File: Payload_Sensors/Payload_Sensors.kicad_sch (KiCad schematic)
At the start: 54 parts, among them J1 Conn_01x06_Pin, U1 MCP9601-E/MX, U2 MCP9601-E/MX, U3 MCP9601-E/MX, U4 MCP9601-E/MX, U5 MCP9601-E/MX

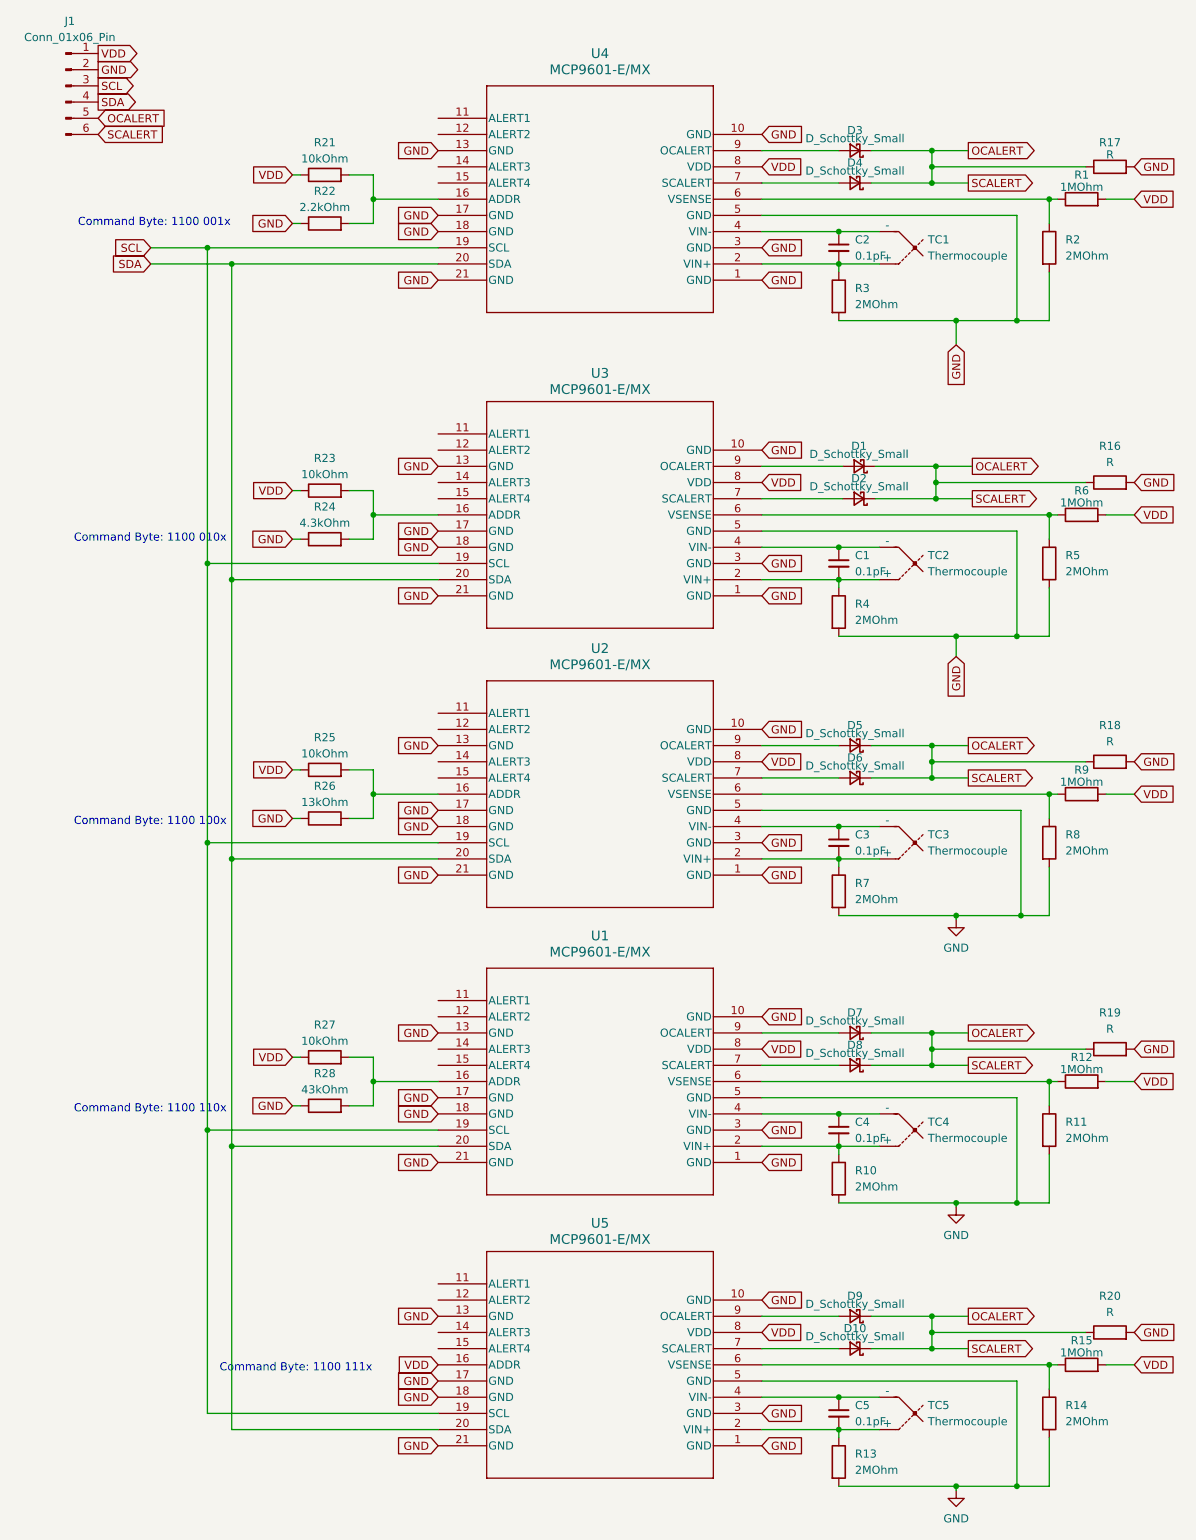
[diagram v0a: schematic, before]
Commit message: using hierarchical sheet
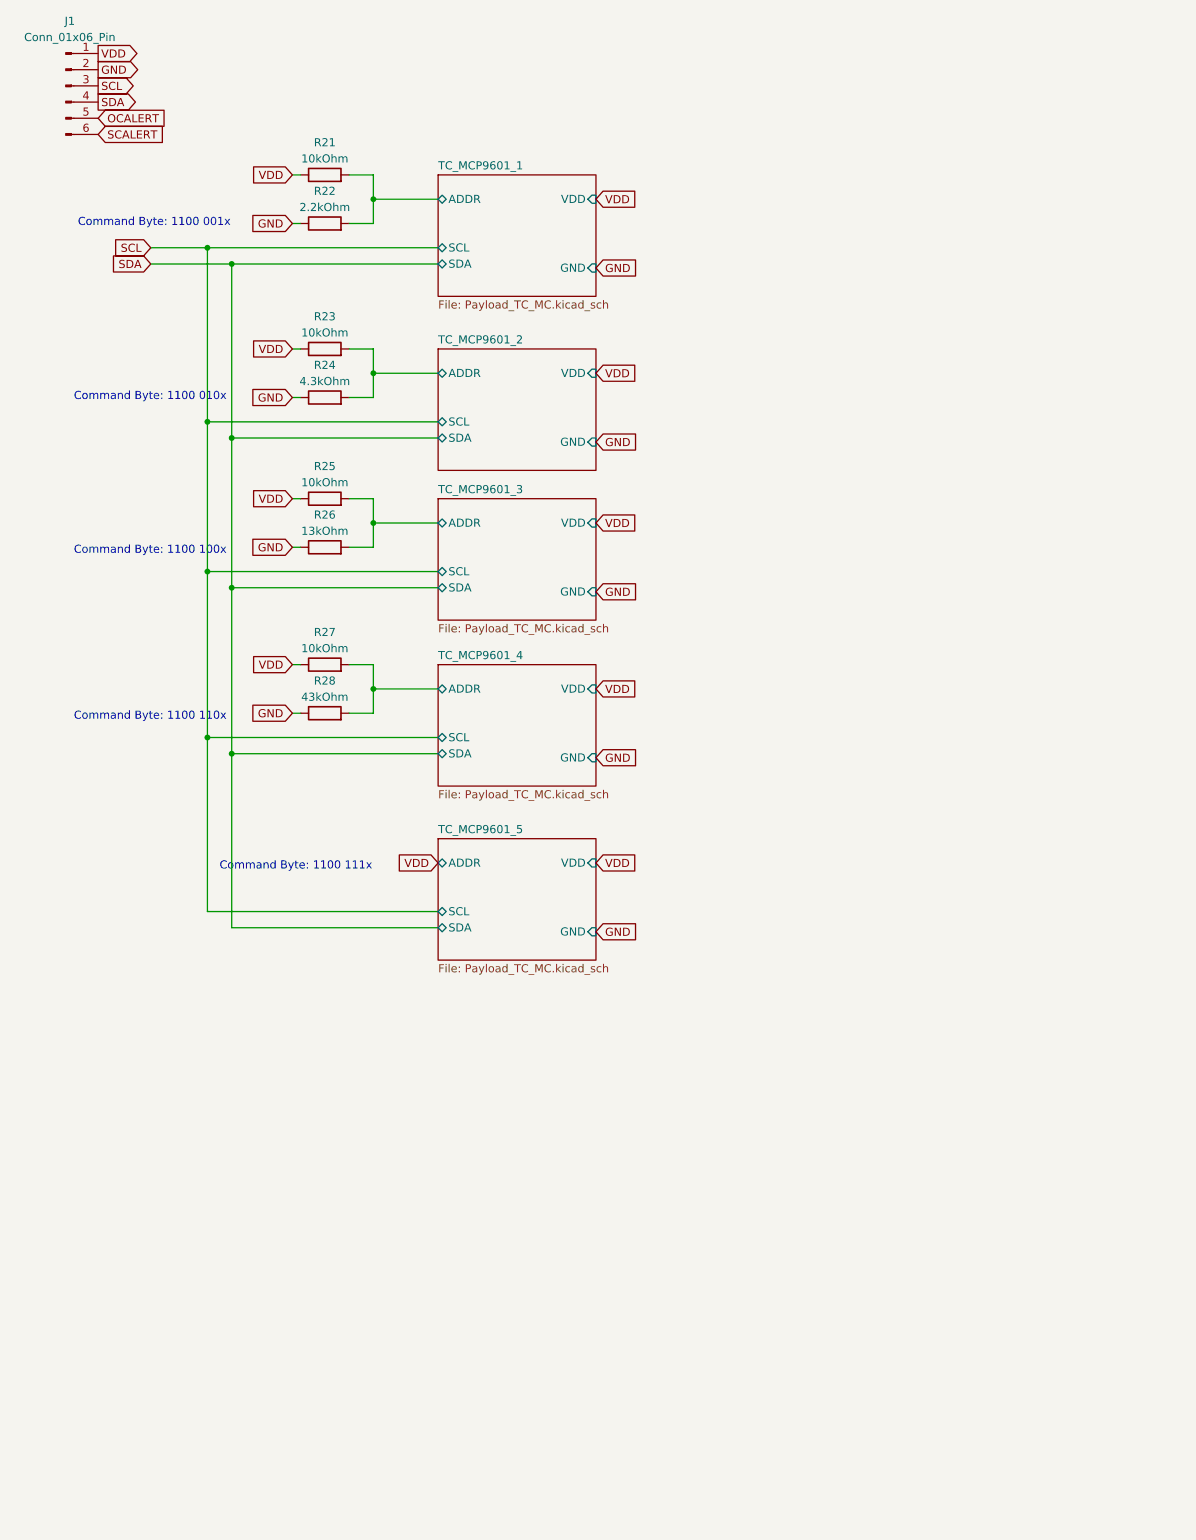
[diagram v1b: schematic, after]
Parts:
- removed C1, C2, C3, C4, C5: 0.1pF, symbol Device:C_Small
- removed D1, D10, D2, D3, D4, D5, D6, D7, D8, D9: D_Schottky_Small, symbol Device:D_Schottky_Small
- removed R1, R12, R15, R6, R9: 1MOhm, symbol Device:R
- removed R10, R11, R13, R14, R2, R3, R4, R5, R7, R8: 2MOhm, symbol Device:R
- removed R16, R17, R18, R19, R20: R, symbol Device:R
- removed TC1, TC2, TC3, TC4, TC5: Thermocouple, symbol Device:Thermocouple
- removed U1, U2, U3, U4, U5: MCP9601-E/MX, MQFN20_NU_MCH, symbol Private:MCP9601-E_MX
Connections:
- net OCALERT: no longer J1.6 (Pin_6)
- net TC_MCP9601_2/ADDR: now reaches R23.2, R24.2
- net TC_MCP9601_1/ADDR: now reaches R21.2, R22.2
- net TC_MCP9601_4/ADDR: now reaches R27.2, R28.2
- net TC_MCP9601_3/ADDR: now reaches R25.2, R26.2
- new net SCALERT: J1.6 (Pin_6)
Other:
- added sheet TC_MCP9601_1 (Payload_TC_MC.kicad_sch)
- added sheet TC_MCP9601_2 (Payload_TC_MC.kicad_sch)
- added sheet TC_MCP9601_3 (Payload_TC_MC.kicad_sch)
- added sheet TC_MCP9601_4 (Payload_TC_MC.kicad_sch)
- added sheet TC_MCP9601_5 (Payload_TC_MC.kicad_sch)
- moved on the sheet: R23, R24, R25, R26, R27, R28
